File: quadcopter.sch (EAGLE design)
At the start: 63 parts, among them J1 ISP, M1 MOTOR_PADS, M2 MOTOR_PADS, M3 MOTOR_PADS, M4 MOTOR_PADS, U1 ATMEGA128RFA1

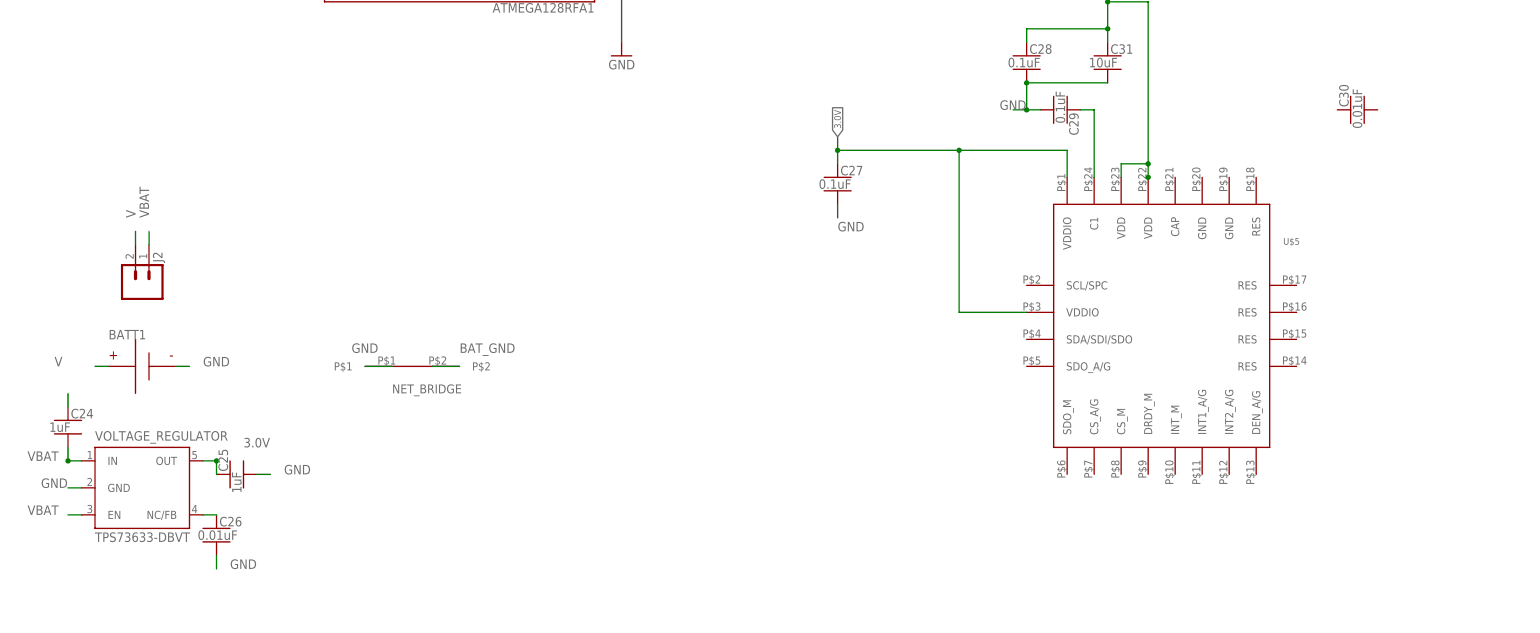
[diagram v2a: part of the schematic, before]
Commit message: IMU finished, LED lib added but empty
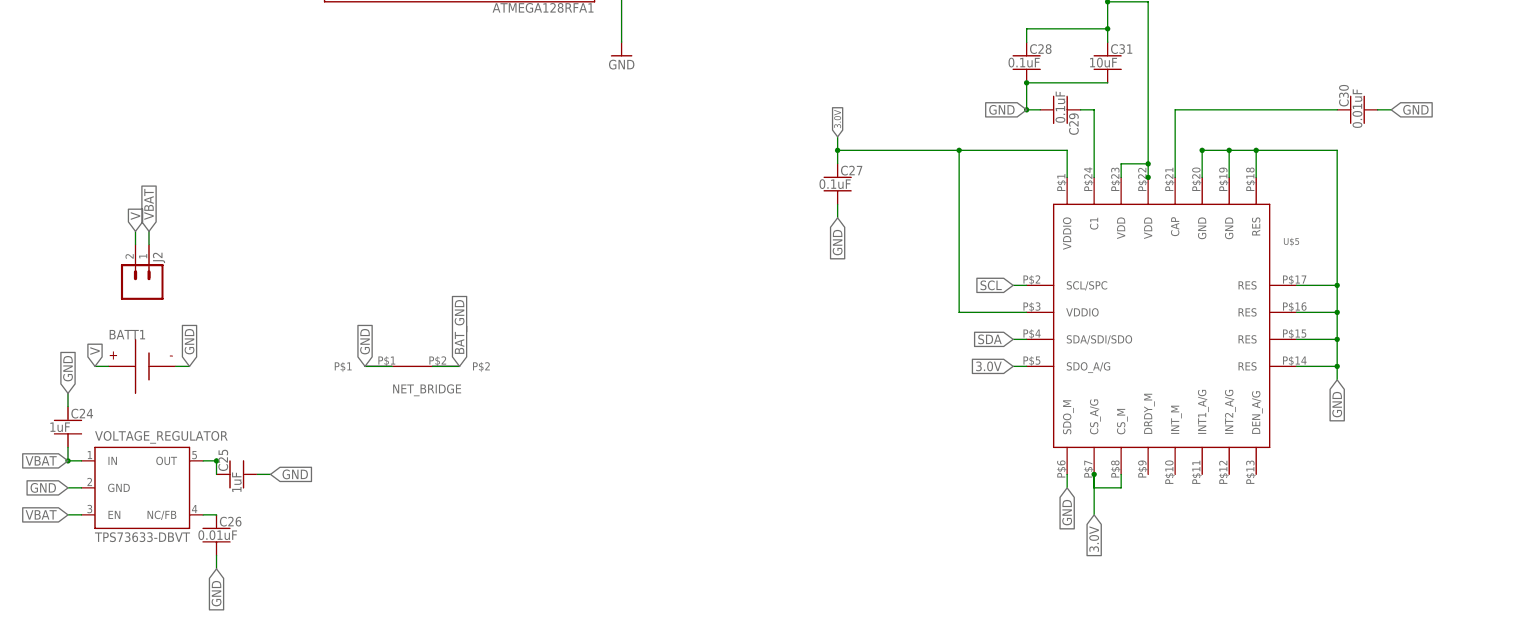
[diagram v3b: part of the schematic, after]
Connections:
- removed net N$1: C24.1
- new net N$2: C30.1, U$5.CAP
- net 3.0V: now also U$5.CS_A/G, U$5.CS_M, U$5.SDO_A/G
- net GND: now also C24.1, C30.2, U$5.GND@1, U$5.GND@2, U$5.RES@1, U$5.RES@2, U$5.RES@3, U$5.RES@4, U$5.RES@5, U$5.SDO_M
- net SCL: now also U$5.SCL/SPC
- net SDA: now also U$5.SDA/SDI/SDO
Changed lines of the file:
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@@
 <?xml version="1.0" encoding="utf-8"?>
 <!DOCTYPE eagle SYSTEM "eagle.dtd">
-<eagle version="8.1.1">
+<eagle version="8.1.0">
 <drawing>
 <settings>
@@
 <pinref part="BATT1" gate="G$1" pin="N"/>
 <wire x1="7.62" y1="-53.34" x2="10.16" y2="-53.34" width="0.1524" layer="91"/>
-<label x="12.7" y="-53.34" size="1.778" layer="95"/>
+<label x="10.16" y="-53.34" size="1.778" layer="95" rot="R90" xref="yes"/>
 </segment>
 <segment>
 <pinref part="NET_BRIDGE" gate="G$1" pin="P$1"/>
 <wire x1="48.26" y1="-53.34" x2="43.18" y2="-53.34" width="0.1524" layer="91"/>
-<label x="40.64" y="-50.8" size="1.778" layer="95"/>
+<label x="43.18" y="-53.34" size="1.778" layer="95" rot="R90" xref="yes"/>
 </segment>
 <segment>
 <pinref part="VOLTAGE_REGULATOR" gate="G$1" pin="GND"/>
 <wire x1="-10.16" y1="-76.2" x2="-12.7" y2="-76.2" width="0.1524" layer="91"/>
-<label x="-17.78" y="-76.2" size="1.778" layer="95"/>
+<label x="-12.7" y="-76.2" size="1.778" layer="95" rot="R180" xref="yes"/>
 </segment>
 <segment>
 <pinref part="C25" gate="G$1" pin="2"/>
 <wire x1="22.86" y1="-73.66" x2="25.4" y2="-73.66" width="0.1524" layer="91"/>
-<label x="27.94" y="-73.66" size="1.778" layer="95"/>
+<label x="25.4" y="-73.66" size="1.778" layer="95" xref="yes"/>
 </segment>
 <segment>
 <pinref part="C26" gate="G$1" pin="2"/>
 <wire x1="15.24" y1="-88.9" x2="15.24" y2="-91.44" width="0.1524" layer="91"/>
-<label x="17.78" y="-91.44" size="1.778" layer="95"/>
+<label x="15.24" y="-91.44" size="1.778" layer="95" rot="R270" xref="yes"/>
 </segment>
 <segment>
 <pinref part="C27" gate="G$1" pin="2"/>
 <wire x1="132.08" y1="-22.86" x2="132.08" y2="-25.4" width="0.1524" layer="91"/>
-<label x="132.08" y="-27.94" size="1.778" layer="95"/>
+<label x="132.08" y="-25.4" size="1.778" layer="95" rot="R270" xref="yes"/>
 </segment>
 <segment>
@@
 <wire x1="167.64" y1="0" x2="182.88" y2="0" width="0.1524" layer="91"/>
 <junction x="167.64" y="0"/>
-<wire x1="167.64" y1="-5.08" x2="165.1" y2="-5.08" width="0.1524" layer="91"/>
 <junction x="167.64" y="-5.08"/>
-<label x="162.56" y="-5.08" size="1.778" layer="95"/>
+<label x="167.64" y="-5.08" size="1.778" layer="95" rot="R180" xref="yes"/>
 </segment>
 <segment>
@@
 <wire x1="297.18" y1="-15.24" x2="307.34" y2="-15.24" width="0.1524" layer="91"/>
 <label x="307.34" y="-15.24" size="1.27" layer="95" xref="yes"/>
+</segment>
+<segment>
+<pinref part="C30" gate="G$1" pin="2"/>
+<wire x1="233.68" y1="-5.08" x2="236.22" y2="-5.08" width="0.1524" layer="91"/>
+<label x="236.22" y="-5.08" size="1.778" layer="95" xref="yes"/>
+</segment>
+<segment>
+<pinref part="U$5" gate="G$1" pin="GND@2"/>
+<wire x1="200.66" y1="-17.78" x2="200.66" y2="-12.7" width="0.1524" layer="91"/>
+<pinref part="U$5" gate="G$1" pin="GND@1"/>
+<wire x1="200.66" y1="-12.7" x2="205.74" y2="-12.7" width="0.1524" layer="91"/>
+<wire x1="205.74" y1="-12.7" x2="205.74" y2="-17.78" width="0.1524" layer="91"/>
+<pinref part="U$5" gate="G$1" pin="RES@5"/>
+<wire x1="205.74" y1="-12.7" x2="210.82" y2="-12.7" width="0.1524" layer="91"/>
+<wire x1="210.82" y1="-12.7" x2="210.82" y2="-17.78" width="0.1524" layer="91"/>
+<junction x="205.74" y="-12.7"/>
+<wire x1="210.82" y1="-12.7" x2="226.06" y2="-12.7" width="0.1524" layer="91"/>
+<wire x1="226.06" y1="-12.7" x2="226.06" y2="-38.1" width="0.1524" layer="91"/>
+<junction x="210.82" y="-12.7"/>
+<pinref part="U$5" gate="G$1" pin="RES@4"/>
+<wire x1="226.06" y1="-38.1" x2="226.06" y2="-43.18" width="0.1524" layer="91"/>
+<wire x1="226.06" y1="-43.18" x2="226.06" y2="-48.26" width="0.1524" layer="91"/>
+<wire x1="226.06" y1="-48.26" x2="226.06" y2="-53.34" width="0.1524" layer="91"/>
+<wire x1="226.06" y1="-53.34" x2="226.06" y2="-55.88" width="0.1524" layer="91"/>
+<wire x1="218.44" y1="-38.1" x2="226.06" y2="-38.1" width="0.1524" layer="91"/>
+<junction x="226.06" y="-38.1"/>
+<pinref part="U$5" gate="G$1" pin="RES@3"/>
+<wire x1="218.44" y1="-43.18" x2="226.06" y2="-43.18" width="0.1524" layer="91"/>
+<junction x="226.06" y="-43.18"/>
+<pinref part="U$5" gate="G$1" pin="RES@2"/>
+<wire x1="218.44" y1="-48.26" x2="226.06" y2="-48.26" width="0.1524" layer="91"/>
+<junction x="226.06" y="-48.26"/>
+<pinref part="U$5" gate="G$1" pin="RES@1"/>
+<wire x1="218.44" y1="-53.34" x2="226.06" y2="-53.34" width="0.1524" layer="91"/>
+<junction x="226.06" y="-53.34"/>
+<junction x="200.66" y="-12.7"/>
+<label x="226.06" y="-55.88" size="1.778" layer="95" rot="R270" xref="yes"/>
+</segment>
+<segment>
+<pinref part="C24" gate="G$1" pin="1"/>
+<wire x1="-12.7" y1="-60.96" x2="-12.7" y2="-58.42" width="0.1524" layer="91"/>
+<label x="-12.7" y="-58.42" size="1.778" layer="95" rot="R90" xref="yes"/>
+</segment>
+<segment>
+<pinref part="U$5" gate="G$1" pin="SDO_M"/>
+<wire x1="175.26" y1="-73.66" x2="175.26" y2="-76.2" width="0.1524" layer="91"/>
+<label x="175.26" y="-76.2" size="1.778" layer="95" rot="R270" xref="yes"/>
 </segment>
 </net>
@@
 <label x="307.34" y="-35.56" size="1.27" layer="95" xref="yes"/>
 </segment>
+<segment>
+<pinref part="U$5" gate="G$1" pin="SDA/SDI/SDO"/>
+<wire x1="167.64" y1="-48.26" x2="165.1" y2="-48.26" width="0.1524" layer="91"/>
+<label x="165.1" y="-48.26" size="1.778" layer="95" rot="R180" xref="yes"/>
+</segment>
 </net>
 <net name="SCL" class="0">
@@
 <wire x1="297.18" y1="-38.1" x2="307.34" y2="-38.1" width="0.1524" layer="91"/>
 <label x="307.34" y="-38.1" size="1.27" layer="95" xref="yes"/>
+</segment>
+<segment>
+<pinref part="U$5" gate="G$1" pin="SCL/SPC"/>
+<wire x1="167.64" y1="-38.1" x2="165.1" y2="-38.1" width="0.1524" layer="91"/>
+<label x="165.1" y="-38.1" size="1.778" layer="95" rot="R180" xref="yes"/>
 </segment>
 </net>
@@
 <pinref part="C24" gate="G$1" pin="2"/>
 <wire x1="-12.7" y1="-68.58" x2="-12.7" y2="-71.12" width="0.1524" layer="91"/>
-<label x="-20.32" y="-71.12" size="1.778" layer="95"/>
+<label x="-12.7" y="-71.12" size="1.778" layer="95" rot="R180" xref="yes"/>
 </segment>
 <segment>
 <pinref part="VOLTAGE_REGULATOR" gate="G$1" pin="EN"/>
 <wire x1="-10.16" y1="-81.28" x2="-12.7" y2="-81.28" width="0.1524" layer="91"/>
-<label x="-20.32" y="-81.28" size="1.778" layer="95"/>
+<label x="-12.7" y="-81.28" size="1.778" layer="95" rot="R180" xref="yes"/>
 </segment>
 <segment>
 <pinref part="J2" gate="G$1" pin="1"/>
 <wire x1="2.54" y1="-30.48" x2="2.54" y2="-27.94" width="0.1524" layer="91"/>
-<label x="2.54" y="-25.4" size="1.778" layer="95" rot="R90"/>
+<label x="2.54" y="-27.94" size="1.778" layer="95" rot="R90" xref="yes"/>
 </segment>
 <segment>
@@
 <pinref part="VOLTAGE_REGULATOR" gate="G$1" pin="OUT"/>
 <wire x1="12.7" y1="-71.12" x2="15.24" y2="-71.12" width="0.1524" layer="91"/>
-<label x="20.32" y="-68.58" size="1.778" layer="95"/>
 <junction x="15.24" y="-71.12"/>
 <wire x1="15.24" y1="-71.12" x2="15.24" y2="-73.66" width="0.1524" layer="91"/>
@@
 <label x="307.34" y="-22.86" size="1.27" layer="95" xref="yes"/>
 </segment>
+<segment>
+<pinref part="U$5" gate="G$1" pin="CS_M"/>
+<wire x1="185.42" y1="-73.66" x2="185.42" y2="-76.2" width="0.1524" layer="91"/>
+<pinref part="U$5" gate="G$1" pin="CS_A/G"/>
+<wire x1="185.42" y1="-76.2" x2="180.34" y2="-76.2" width="0.1524" layer="91"/>
+<wire x1="180.34" y1="-76.2" x2="180.34" y2="-73.66" width="0.1524" layer="91"/>
+<wire x1="180.34" y1="-73.66" x2="180.34" y2="-81.28" width="0.1524" layer="91"/>
+<junction x="180.34" y="-73.66"/>
+<label x="180.34" y="-81.28" size="1.778" layer="95" rot="R270" xref="yes"/>
+</segment>
+<segment>
+<pinref part="U$5" gate="G$1" pin="SDO_A/G"/>
+<wire x1="167.64" y1="-53.34" x2="165.1" y2="-53.34" width="0.1524" layer="91"/>
+<label x="165.1" y="-53.34" size="1.778" layer="95" rot="R180" xref="yes"/>
+</segment>
 </net>
 <net name="N$18" class="0">
@@
 <pinref part="NET_BRIDGE" gate="G$1" pin="P$2"/>
 <wire x1="55.88" y1="-53.34" x2="60.96" y2="-53.34" width="0.1524" layer="91"/>
-<label x="60.96" y="-50.8" size="1.778" layer="95"/>
+<label x="60.96" y="-53.34" size="1.778" layer="95" rot="R90" xref="yes"/>
 </segment>
 <segment>
@@
 </segment>
 </net>
-<net name="N$1" class="0">
-<segment>
-<pinref part="C24" gate="G$1" pin="1"/>
-<wire x1="-12.7" y1="-60.96" x2="-12.7" y2="-58.42" width="0.1524" layer="91"/>
-</segment>
-</net>
 <net name="V" class="0">
 <segment>
 <pinref part="BATT1" gate="G$1" pin="P"/>
 <wire x1="-5.08" y1="-53.34" x2="-7.62" y2="-53.34" width="0.1524" layer="91"/>
-<label x="-15.24" y="-53.34" size="1.778" layer="95"/>
+<label x="-7.62" y="-53.34" size="1.778" layer="95" rot="R90" xref="yes"/>
 </segment>
 <segment>
 <pinref part="J2" gate="G$1" pin="2"/>
 <wire x1="0" y1="-30.48" x2="0" y2="-27.94" width="0.1524" layer="91"/>
-<label x="0" y="-25.4" size="1.778" layer="95" rot="R90"/>
+<label x="0" y="-27.94" size="1.778" layer="95" rot="R90" xref="yes"/>
 </segment>
 </net>
@@
 </segment>
 </net>
+<net name="N$2" class="0">
+<segment>
+<pinref part="U$5" gate="G$1" pin="CAP"/>
+<pinref part="C30" gate="G$1" pin="1"/>
+<wire x1="195.58" y1="-17.78" x2="195.58" y2="-5.08" width="0.1524" layer="91"/>
+<wire x1="195.58" y1="-5.08" x2="226.06" y2="-5.08" width="0.1524" layer="91"/>
+</segment>
+</net>

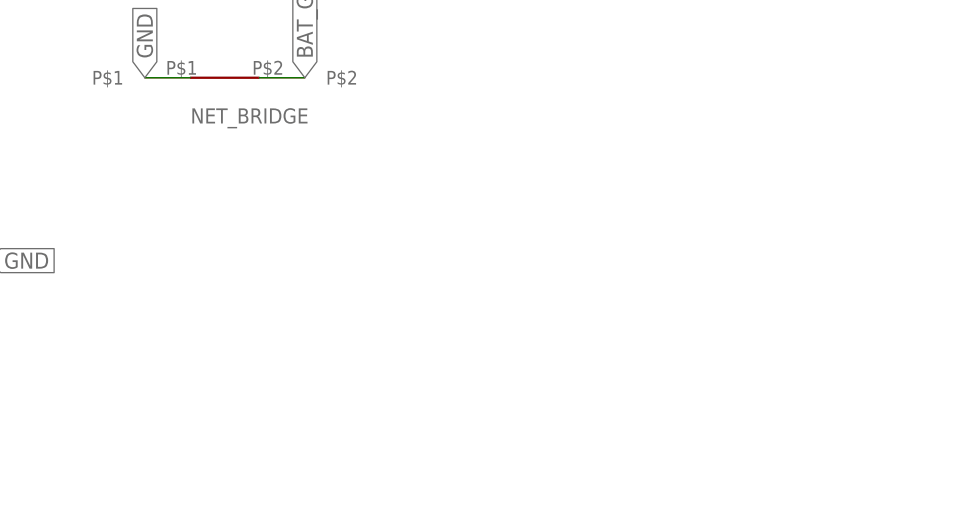
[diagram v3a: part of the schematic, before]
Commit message: Added LEDs into schematic in series, no resistor necessary
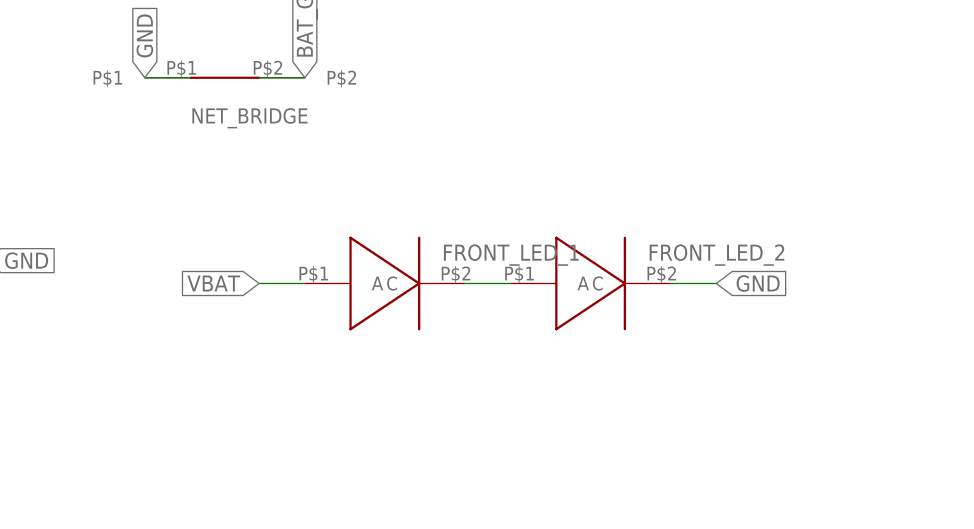
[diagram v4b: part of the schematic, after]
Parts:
- added FRONT_LED_1, FRONT_LED_2: (no value), LEDs:LED-0805-GREEN
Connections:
- new net N$5: FRONT_LED_1.C, FRONT_LED_2.A
- net GND: now also FRONT_LED_2.C
- net VBAT: now also FRONT_LED_1.A
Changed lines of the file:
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@@
 <part name="B2" library="quadparts_prebuilt" deviceset="BALUN" device="0805"/>
 <part name="J3" library="quadparts_prebuilt" deviceset="SIP-10_" device="TH-254X10-1"/>
+<part name="FRONT_LED_1" library="LEDs" deviceset="LED" device="-0805-GREEN"/>
+<part name="FRONT_LED_2" library="LEDs" deviceset="LED" device="-0805-GREEN"/>
 </parts>
 <sheets>
@@
 <instance part="B2" gate="G$1" x="142.24" y="81.28" rot="R180"/>
 <instance part="J3" gate="G$1" x="287.02" y="-40.64"/>
+<instance part="FRONT_LED_1" gate="G$1" x="71.12" y="-76.2"/>
+<instance part="FRONT_LED_2" gate="G$1" x="93.98" y="-76.2"/>
 </instances>
 <busses>
@@
 <label x="175.26" y="-76.2" size="1.778" layer="95" rot="R270" xref="yes"/>
 </segment>
+<segment>
+<pinref part="FRONT_LED_2" gate="G$1" pin="C"/>
+<wire x1="101.6" y1="-76.2" x2="106.68" y2="-76.2" width="0.1524" layer="91"/>
+<label x="106.68" y="-76.2" size="1.778" layer="95" xref="yes"/>
+</segment>
 </net>
 <net name="N$3" class="0">
@@
 <wire x1="297.18" y1="-20.32" x2="307.34" y2="-20.32" width="0.1524" layer="91"/>
 <label x="307.34" y="-20.32" size="1.27" layer="95" xref="yes"/>
+</segment>
+<segment>
+<pinref part="FRONT_LED_1" gate="G$1" pin="A"/>
+<wire x1="60.96" y1="-76.2" x2="55.88" y2="-76.2" width="0.1524" layer="91"/>
+<label x="55.88" y="-76.2" size="1.778" layer="95" rot="R180" xref="yes"/>
 </segment>
 </net>
@@
 </segment>
 </net>
+<net name="N$5" class="0">
+<segment>
+<pinref part="FRONT_LED_1" gate="G$1" pin="C"/>
+<pinref part="FRONT_LED_2" gate="G$1" pin="A"/>
+<wire x1="78.74" y1="-76.2" x2="83.82" y2="-76.2" width="0.1524" layer="91"/>
+</segment>
+</net>
